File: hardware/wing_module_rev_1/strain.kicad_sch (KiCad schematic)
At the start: 15 parts, among them J5 STRAIN, J6 TORSION, U5 ADS131M03IRUK

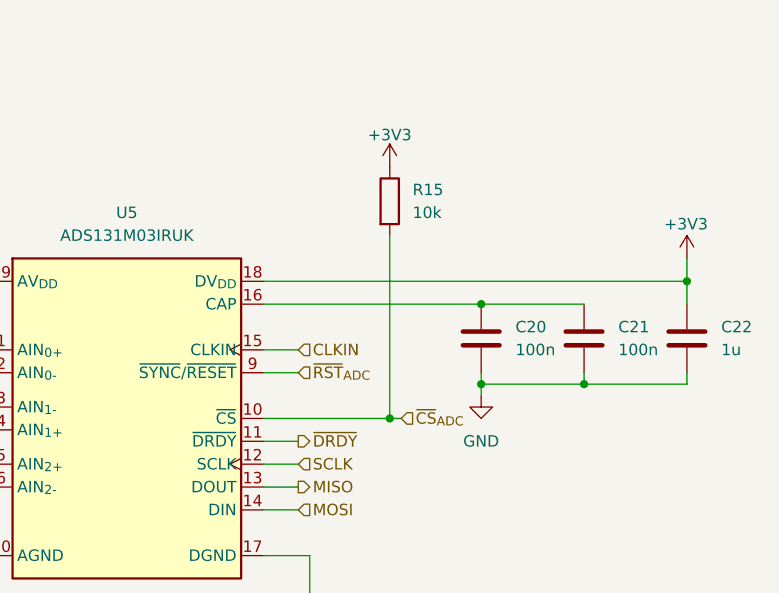
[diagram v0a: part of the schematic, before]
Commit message: Finished rev 1.0 layout of CAN
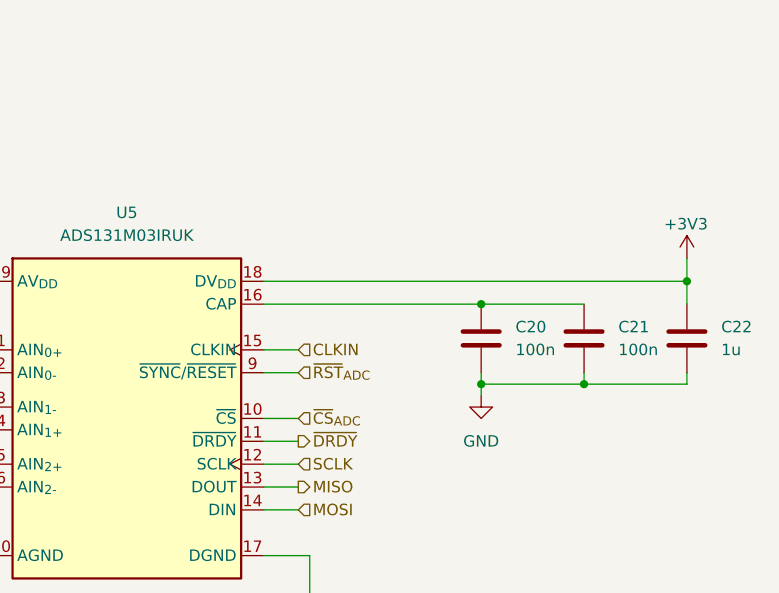
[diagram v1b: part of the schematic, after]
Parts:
- removed R15: 10k, Resistor_SMD:R_0402_1005Metric, symbol Device:R
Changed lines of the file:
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@@
-	)
-	(junction
-		(at 198.12 92.71)
-		(diameter 0)
-		(color 0 0 0 0)
 	)
 	(junction
@@
 	(wire
 		(pts
-			(xy 199.39 92.71) (xy 198.12 92.71)
+			(xy 184.15 92.71) (xy 187.96 92.71)
 		)
 		(stroke
@@
 		(pts
 			(xy 90.17 80.01) (xy 92.71 80.01)
-		)
-		(stroke
-			(width 0)
-			(type default)
-		)
-	)
-	(wire
-		(pts
-			(xy 198.12 72.39) (xy 198.12 92.71)
-		)
-		(stroke
-			(width 0)
-			(type default)
-		)
-	)
-	(wire
-		(pts
-			(xy 184.15 92.71) (xy 198.12 92.71)
 		)
 		(stroke
@@
 	(hierarchical_label "~{CS}_{ADC}"
 		(shape input)
-		(at 199.39 92.71 0)
+		(at 187.96 92.71 0)
 		(effects
 			(font
@@
 	(symbol
 		(lib_id "Device:R")
-		(at 198.12 68.58 0)
-		(unit 1)
-		(exclude_from_sim no)
-		(in_bom yes)
-		(on_board yes)
-		(dnp no)
-		(fields_autoplaced yes)
-		(property "Reference" "R15"
-			(at 200.66 67.3099 0)
-			(effects
-				(font
-					(size 1.27 1.27)
-				)
-				(justify left)
-			)
-		)
-		(property "Value" "10k"
-			(at 200.66 69.8499 0)
-			(effects
-				(font
-					(size 1.27 1.27)
-				)
-				(justify left)
-			)
-		)
-		(property "Footprint" "Resistor_SMD:R_0402_1005Metric"
-			(at 196.342 68.58 90)
-			(effects
-				(font
-					(size 1.27 1.27)
-				)
-				(hide yes)
-			)
-		)
-		(property "Datasheet" "~"
-			(at 198.12 68.58 0)
-			(effects
-				(font
-					(size 1.27 1.27)
-				)
-				(hide yes)
-			)
-		)
-		(property "Description" "Resistor"
-			(at 198.12 68.58 0)
-			(effects
-				(font
-					(size 1.27 1.27)
-				)
-				(hide yes)
-			)
-		)
-		(property "LCSC" "C723353"
-			(at 198.12 68.58 0)
-			(effects
-				(font
-					(size 1.27 1.27)
-				)
-				(hide yes)
-			)
-		)
-		(pin "1"
-		)
-		(pin "2"
-		)
-		(instances
-			(project "wing_module_rev_1"
-				(path "/7b7fffa9-e888-4279-94bf-385d74cf78f9/424e4183-41f2-435c-8d3d-5784f425df45"
-					(reference "R15")
-					(unit 1)
-				)
-			)
-		)
-	)
-	(symbol
-		(lib_id "Device:R")
 		(at 99.06 80.01 90)
 		(unit 1)
@@
 					(unit 1)
 				)
-			)
-		)
-	)
-	(symbol
-		(lib_id "power:+3V3")
-		(at 198.12 64.77 0)
-		(mirror y)
-		(unit 1)
-		(exclude_from_sim no)
-		(in_bom yes)
-		(on_board yes)
-		(dnp no)
-		(property "Reference" "#PWR043"
-			(at 198.12 68.58 0)
-			(effects
-				(font
-					(size 1.27 1.27)
-				)
-				(hide yes)
-			)
-		)
-		(property "Value" "+3V3"
-			(at 198.12 61.214 0)
-			(effects
-				(font
-					(size 1.27 1.27)
-				)
-			)
-		)
-		(property "Footprint" ""
-			(at 198.12 64.77 0)
-			(effects
-				(font
-					(size 1.27 1.27)
-				)
-				(hide yes)
-			)
-		)
-		(property "Datasheet" ""
-			(at 198.12 64.77 0)
-			(effects
-				(font
-					(size 1.27 1.27)
-				)
-				(hide yes)
-			)
-		)
-		(property "Description" "Power symbol creates a global label with name \"+3V3\""
-			(at 198.12 64.77 0)
-			(effects
-				(font
-					(size 1.27 1.27)
-				)
-				(hide yes)
-			)
-		)
-		(pin "1"
-		)
-		(instances
-			(project "wing_module_rev_1"
-				(path "/7b7fffa9-e888-4279-94bf-385d74cf78f9/424e4183-41f2-435c-8d3d-5784f425df45"
-					(reference "#PWR043")
-					(unit 1)
-				)

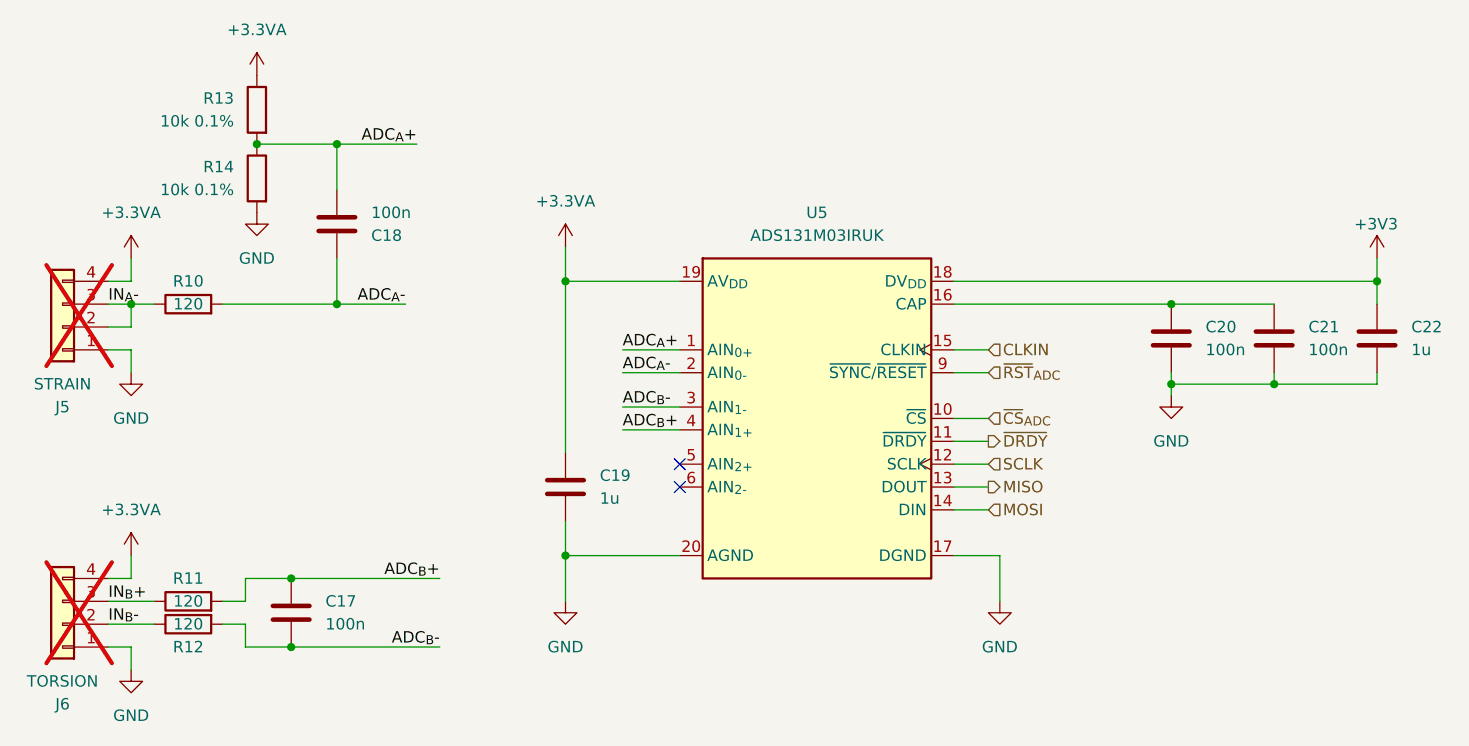
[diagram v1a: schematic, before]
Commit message: Reassigned reference numbers
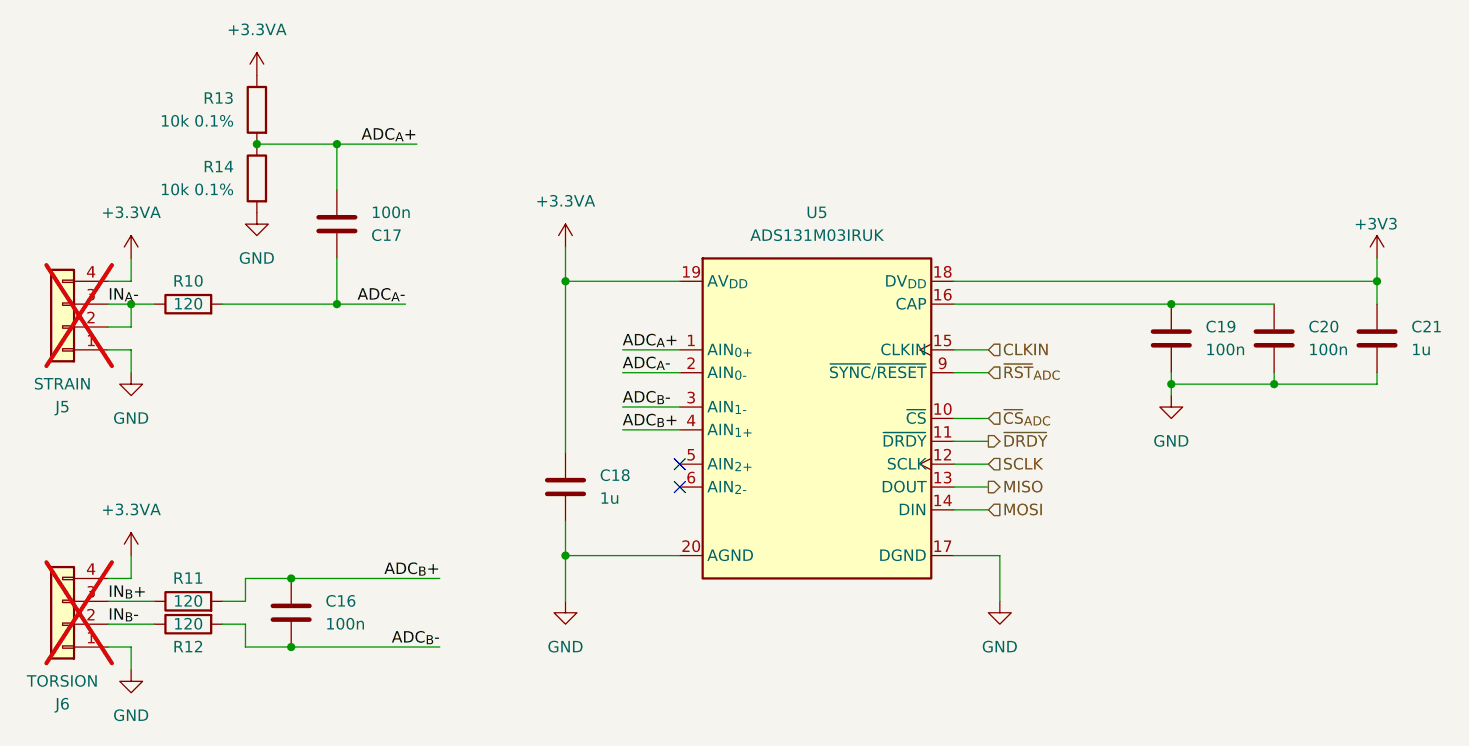
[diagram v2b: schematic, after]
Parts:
- renumbered C17 to C16, C18 to C17, C19 to C18, C20 to C19, C21 to C20, C22 to C21
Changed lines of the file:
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@@
 		(dnp no)
 		(fields_autoplaced yes)
-		(property "Reference" "C17"
+		(property "Reference" "C16"
 			(at 114.3 113.0299 0)
 			(effects
@@
 			(project "wing_module_rev_1"
 				(path "/7b7fffa9-e888-4279-94bf-385d74cf78f9/424e4183-41f2-435c-8d3d-5784f425df45"
-					(reference "C17")
+					(reference "C16")
 					(unit 1)
 				)
@@
 		(dnp no)
 		(fields_autoplaced yes)
-		(property "Reference" "C20"
+		(property "Reference" "C19"
 			(at 212.09 82.5499 0)
 			(effects
@@
 			(project "wing_module_rev_1"
 				(path "/7b7fffa9-e888-4279-94bf-385d74cf78f9/424e4183-41f2-435c-8d3d-5784f425df45"
-					(reference "C20")
+					(reference "C19")
 					(unit 1)
 				)
@@
 		(dnp no)
 		(fields_autoplaced yes)
-		(property "Reference" "#PWR044"
+		(property "Reference" "#PWR043"
 			(at 208.28 96.52 0)
 			(effects
@@
 			(project "wing_module_rev_1"
 				(path "/7b7fffa9-e888-4279-94bf-385d74cf78f9/424e4183-41f2-435c-8d3d-5784f425df45"
-					(reference "#PWR044")
+					(reference "#PWR043")
 					(unit 1)
 				)
@@
 		(on_board yes)
 		(dnp no)
-		(property "Reference" "#PWR045"
+		(property "Reference" "#PWR044"
 			(at 231.14 78.74 0)
 			(effects
@@
 			(project "wing_module_rev_1"
 				(path "/7b7fffa9-e888-4279-94bf-385d74cf78f9/424e4183-41f2-435c-8d3d-5784f425df45"
-					(reference "#PWR045")
+					(reference "#PWR044")
 					(unit 1)
 				)
@@
 		(dnp no)
 		(fields_autoplaced yes)
-		(property "Reference" "C18"
+		(property "Reference" "C17"
 			(at 119.38 72.3901 0)
 			(effects
@@
 			(project "wing_module_rev_1"
 				(path "/7b7fffa9-e888-4279-94bf-385d74cf78f9/424e4183-41f2-435c-8d3d-5784f425df45"
-					(reference "C18")
+					(reference "C17")
 					(unit 1)
 				)
@@
 		(dnp no)
 		(fields_autoplaced yes)
-		(property "Reference" "C22"
+		(property "Reference" "C21"
 			(at 234.95 82.5499 0)
 			(effects
@@
 			(project "wing_module_rev_1"
 				(path "/7b7fffa9-e888-4279-94bf-385d74cf78f9/424e4183-41f2-435c-8d3d-5784f425df45"
-					(reference "C22")
+					(reference "C21")
 					(unit 1)
 				)
@@
 		(dnp no)
 		(fields_autoplaced yes)
-		(property "Reference" "C19"
+		(property "Reference" "C18"
 			(at 144.78 99.0599 0)
 			(effects
@@
 			(project "wing_module_rev_1"
 				(path "/7b7fffa9-e888-4279-94bf-385d74cf78f9/424e4183-41f2-435c-8d3d-5784f425df45"
-					(reference "C19")
+					(reference "C18")
 					(unit 1)
 				)
@@
 		(dnp no)
 		(fields_autoplaced yes)
-		(property "Reference" "C21"
+		(property "Reference" "C20"
 			(at 223.52 82.5499 0)
 			(effects
@@
 			(project "wing_module_rev_1"
 				(path "/7b7fffa9-e888-4279-94bf-385d74cf78f9/424e4183-41f2-435c-8d3d-5784f425df45"
-					(reference "C21")
-					(unit 1)
-				)
+					(reference "C20")
+					(unit 1)
+				)
